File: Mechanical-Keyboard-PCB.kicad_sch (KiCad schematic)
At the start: 1 part, among them U1 ATmega32U4-A

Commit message: UCAP and HWB
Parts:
- added C2: C_Small, symbol Device:C_Small
- added R1: 10K, symbol Device:R_Small
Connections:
- net MOSI: now reaches U1.10 (PB2)
- net MISO: now reaches U1.11 (PB3)
- net RESET: now reaches U1.13 (~{RESET})
- net +5V: now reaches U1.14 (VCC), U1.34 (VCC)
- net +5V: now also U1.2 (UVCC), U1.24 (AVCC), U1.44 (AVCC)
- net GND: now reaches U1.15 (GND), U1.23 (GND), U1.35 (GND), U1.43 (GND)
- net GND: now also U1.5 (UGND), C2.2, R1.2
- net XTAL2: now reaches U1.16 (XTAL2)
- net XTAL1: now reaches U1.17 (XTAL1)
- net D-: now reaches U1.3 (D-)
- net at U1.33 (~{HWB}/PE2): now also R1.1
- net D+: now reaches U1.4 (D+)
- net at U1.6 (UCAP): now also C2.1
- net SCK: now reaches U1.9 (PB1)
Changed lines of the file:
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@@
 (kicad_sch (version 20230121) (generator eeschema)
   (paper "A4")
+  (junction (at 212.09 38.1) (diameter 0) (color 0 0 0 0)
+  )
+  (junction (at 209.55 129.54) (diameter 0) (color 0 0 0 0)
+  )
+  (junction (at 209.55 38.1) (diameter 0) (color 0 0 0 0)
+  )
+  (wire (pts (xy 212.09 38.1) (xy 214.63 38.1))
+    (stroke (width 0) (type default))
+  )
+  (wire (pts (xy 199.39 129.54) (xy 209.55 129.54))
+    (stroke (width 0) (type default))
+  )
+  (wire (pts (xy 248.92 99.06) (xy 261.62 99.06))
+    (stroke (width 0) (type default))
+  )
+  (wire (pts (xy 209.55 38.1) (xy 212.09 38.1))
+    (stroke (width 0) (type default))
+  )
+  (wire (pts (xy 199.39 134.62) (xy 199.39 129.54))
+    (stroke (width 0) (type default))
+  )
+  (wire (pts (xy 196.85 78.74) (xy 185.42 78.74))
+    (stroke (width 0) (type default))
+  )
+  (wire (pts (xy 209.55 33.02) (xy 209.55 38.1))
+    (stroke (width 0) (type default))
+  )
+  (wire (pts (xy 227.33 99.06) (xy 243.84 99.06))
+    (stroke (width 0) (type default))
+  )
+  (wire (pts (xy 261.62 99.06) (xy 261.62 101.6))
+    (stroke (width 0) (type default))
+  )
+  (wire (pts (xy 185.42 78.74) (xy 185.42 92.71))
+    (stroke (width 0) (type default))
+  )
+  (wire (pts (xy 209.55 129.54) (xy 212.09 129.54))
+    (stroke (width 0) (type default))
+  )
+  (hierarchical_label "MISO" (shape input) (at 227.33 53.34 0) (fields_autoplaced)
+    (effects (font (size 1.27 1.27)) (justify left))
+  )
+  (hierarchical_label "D+" (shape input) (at 196.85 71.12 180) (fields_autoplaced)
+    (effects (font (size 1.27 1.27)) (justify right))
+  )
+  (hierarchical_label "XTAL2" (shape input) (at 196.85 55.88 180) (fields_autoplaced)
+    (effects (font (size 1.27 1.27)) (justify right))
+  )
+  (hierarchical_label "D-" (shape input) (at 196.85 73.66 180) (fields_autoplaced)
+    (effects (font (size 1.27 1.27)) (justify right))
+  )
+  (hierarchical_label "XTAL1" (shape input) (at 196.85 50.8 180) (fields_autoplaced)
+    (effects (font (size 1.27 1.27)) (justify right))
+  )
+  (hierarchical_label "SCK" (shape input) (at 227.33 48.26 0) (fields_autoplaced)
+    (effects (font (size 1.27 1.27)) (justify left))
+  )
+  (hierarchical_label "RESET" (shape input) (at 196.85 45.72 180) (fields_autoplaced)
+    (effects (font (size 1.27 1.27)) (justify right))
+  )
+  (hierarchical_label "MOSI" (shape input) (at 227.33 50.8 0) (fields_autoplaced)
+    (effects (font (size 1.27 1.27)) (justify left))
+  )
+  (symbol (lib_id "Device:C_Small") (at 185.42 95.25 0) (unit 1)
+    (in_bom yes) (on_board yes) (dnp no) (fields_autoplaced)
+    (property "Reference" "C2" (at 187.96 94.6213 0)
+      (effects (font (size 1.27 1.27)) (justify left))
+    )
+    (property "Value" "C_Small" (at 187.96 97.1613 0)
+      (effects (font (size 1.27 1.27)) (justify left))
+    )
+    (property "Footprint" "" (at 185.42 95.25 0)
+      (effects (font (size 1.27 1.27)) hide)
+    )
+    (property "Datasheet" "~" (at 185.42 95.25 0)
+      (effects (font (size 1.27 1.27)) hide)
+    )
+    (pin "1")
+    (pin "2")
+    (instances
+      (project "Mechanical-Keyboard-PCB"
+        (path "/99e75afe-79a0-48d3-af4c-243d7dba3013"
+          (reference "C2") (unit 1)
+        )
+      )
+    )
+  )
+  (symbol (lib_id "power:GND") (at 261.62 101.6 0) (unit 1)
+    (in_bom yes) (on_board yes) (dnp no) (fields_autoplaced)
+    (property "Reference" "#PWR04" (at 261.62 107.95 0)
+      (effects (font (size 1.27 1.27)) hide)
+    )
+    (property "Value" "GND" (at 261.62 106.68 0)
+      (effects (font (size 1.27 1.27)))
+    )
+    (property "Footprint" "" (at 261.62 101.6 0)
+      (effects (font (size 1.27 1.27)) hide)
+    )
+    (property "Datasheet" "" (at 261.62 101.6 0)
+      (effects (font (size 1.27 1.27)) hide)
+    )
+    (pin "1")
+    (instances
+      (project "Mechanical-Keyboard-PCB"
+        (path "/99e75afe-79a0-48d3-af4c-243d7dba3013"
+          (reference "#PWR04") (unit 1)
+        )
+      )
+    )
+  )
+  (symbol (lib_id "power:+5V") (at 209.55 33.02 0) (unit 1)
+    (in_bom yes) (on_board yes) (dnp no) (fields_autoplaced)
+    (property "Reference" "#PWR01" (at 209.55 36.83 0)
+      (effects (font (size 1.27 1.27)) hide)
+    )
+    (property "Value" "+5V" (at 209.55 29.21 0)
+      (effects (font (size 1.27 1.27)))
+    )
+    (property "Footprint" "" (at 209.55 33.02 0)
+      (effects (font (size 1.27 1.27)) hide)
+    )
+    (property "Datasheet" "" (at 209.55 33.02 0)
+      (effects (font (size 1.27 1.27)) hide)
+    )
+    (pin "1")
+    (instances
+      (project "Mechanical-Keyboard-PCB"
+        (path "/99e75afe-79a0-48d3-af4c-243d7dba3013"
+          (reference "#PWR01") (unit 1)
+        )
+      )
+    )
+  )
+  (symbol (lib_id "Device:R_Small") (at 246.38 99.06 90) (unit 1)
+    (in_bom yes) (on_board yes) (dnp no) (fields_autoplaced)
+    (property "Reference" "R1" (at 246.38 93.98 90)
+      (effects (font (size 1.27 1.27)))
+    )
+    (property "Value" "10K" (at 246.38 96.52 90)
+      (effects (font (size 1.27 1.27)))
+    )
+    (property "Footprint" "" (at 246.38 99.06 0)
+      (effects (font (size 1.27 1.27)) hide)
+    )
+    (property "Datasheet" "~" (at 246.38 99.06 0)
+      (effects (font (size 1.27 1.27)) hide)
+    )
+    (pin "1")
+    (pin "2")
+    (instances
+      (project "Mechanical-Keyboard-PCB"
+        (path "/99e75afe-79a0-48d3-af4c-243d7dba3013"
+          (reference "R1") (unit 1)
+        )
+      )
+    )
+  )
   (symbol (lib_id "MCU_Microchip_ATmega:ATmega32U4-A") (at 212.09 83.82 0) (unit 1)
     (in_bom yes) (on_board yes) (dnp no) (fields_autoplaced)
@@
         )
       )
+    )
+  )
+  (symbol (lib_id "power:GND") (at 199.39 134.62 0) (unit 1)
+    (in_bom yes) (on_board yes) (dnp no) (fields_autoplaced)
+    (property "Reference" "#PWR02" (at 199.39 140.97 0)
+      (effects (font (size 1.27 1.27)) hide)
+    )
+    (property "Value" "GND" (at 199.39 139.7 0)
+      (effects (font (size 1.27 1.27)))
+    )
+    (property "Footprint" "" (at 199.39 134.62 0)
+      (effects (font (size 1.27 1.27)) hide)
+    )
+    (property "Datasheet" "" (at 199.39 134.62 0)
+      (effects (font (size 1.27 1.27)) hide)
+    )
+    (pin "1")
+    (instances
+      (project "Mechanical-Keyboard-PCB"
+        (path "/99e75afe-79a0-48d3-af4c-243d7dba3013"
+          (reference "#PWR02") (unit 1)
+        )
+      )
+    )
+  )
+  (symbol (lib_id "power:GND") (at 185.42 97.79 0) (unit 1)
+    (in_bom yes) (on_board yes) (dnp no) (fields_autoplaced)
+    (property "Reference" "#PWR03" (at 185.42 104.14 0)
+      (effects (font (size 1.27 1.27)) hide)
+    )
+    (property "Value" "GND" (at 185.42 102.87 0)
+      (effects (font (size 1.27 1.27)))
+    )
+    (property "Footprint" "" (at 185.42 97.79 0)
+      (effects (font (size 1.27 1.27)) hide)
+    )
+    (property "Datasheet" "" (at 185.42 97.79 0)
+      (effects (font (size 1.27 1.27)) hide)
+    )
+    (pin "1")
+    (instances
+      (project "Mechanical-Keyboard-PCB"
+        (path "/99e75afe-79a0-48d3-af4c-243d7dba3013"
+          (reference "#PWR03") (unit 1)
+        )
+      )

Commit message: Crystal, decoupling capacitors + ISP
Crystal, decoupling capacitors + ISP
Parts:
- added C1, C3: 22p, symbol Device:C_Small
- added C1, C2, C3, C4: 0.1u, symbol Device:C_Small
- added C5: 10u, symbol Device:C_Small
- added J1: AVR-ISP-6, symbol Connector:AVR-ISP-6
- added XTAL: X?, symbol Device:Crystal_GND24_Small
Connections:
- net +5V: now also C1.1, C1.2, C1.2, C2.1, C2.2, C3.1, C3.2, C3.2, C4.1, C4.2, C5.1, C5.2, J1.2 (VCC), J1.6 (GND), XTAL.2, XTAL.4
- net MISO: now also J1.1 (MISO)
- net MOSI: now also J1.4 (MOSI)
- net RESET: now also J1.5 (~{RST})
- net SCK: now also J1.3 (SCK)
- net XTAL1: now also C1.1, XTAL.1
- net XTAL2: now also C3.1, XTAL.3
- no-connect marks 0 -> 1

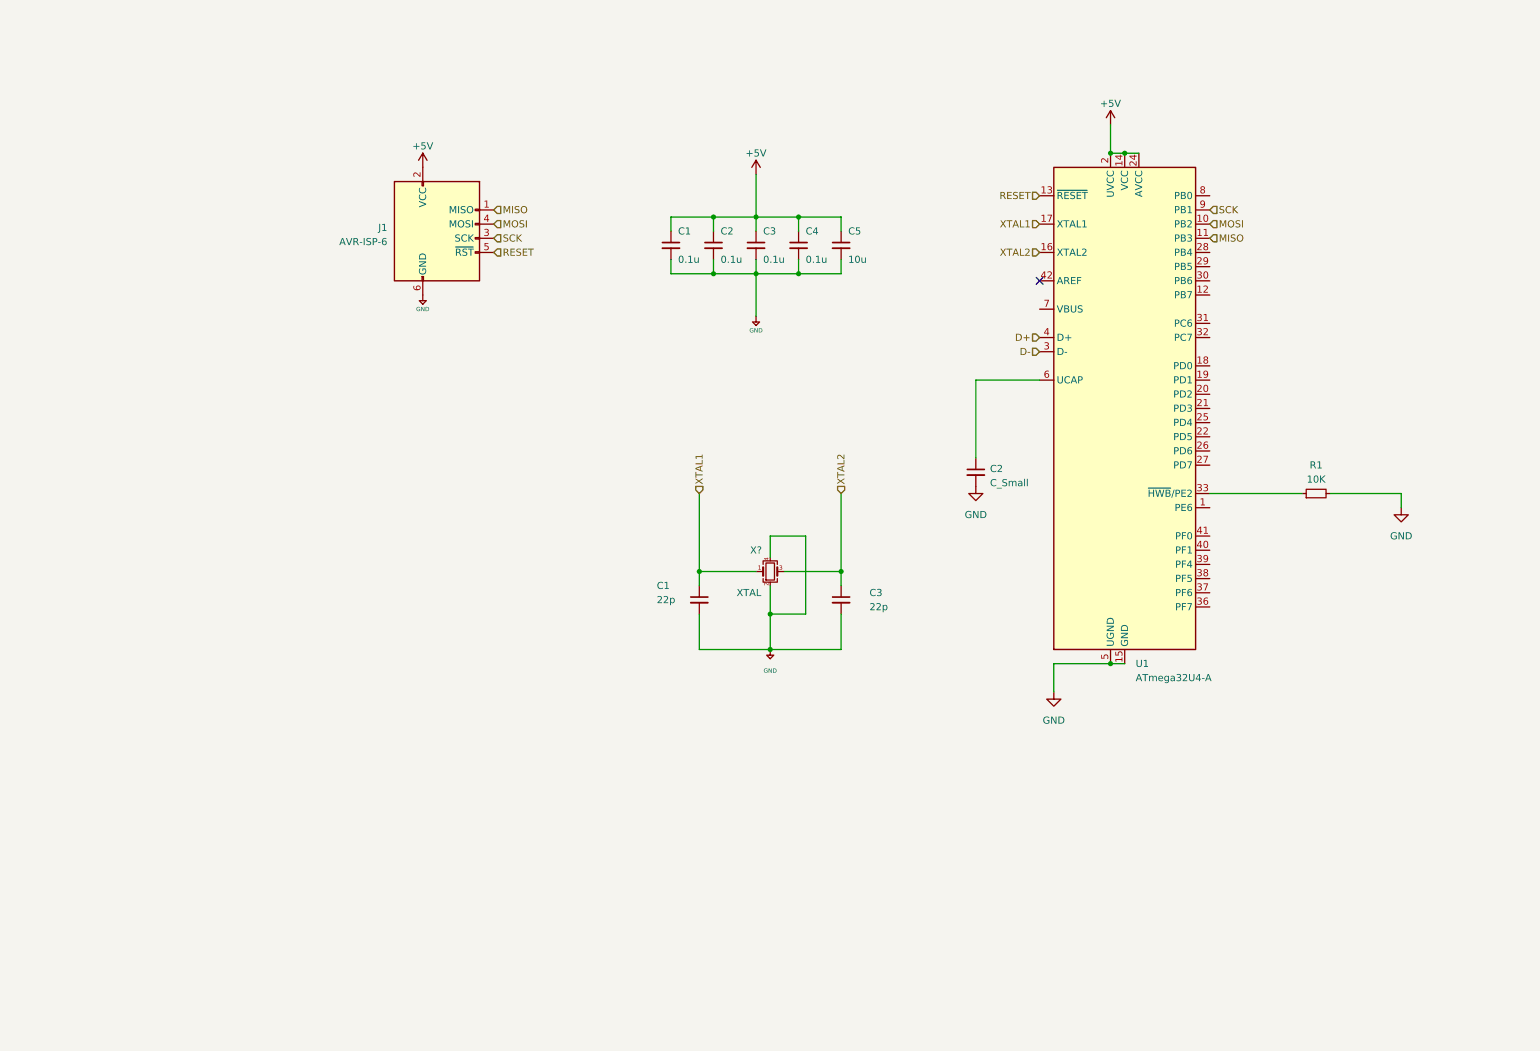
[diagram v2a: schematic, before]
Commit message: Schematic - USB, EMI + RESET
Added USB, EMI + RESET to the schematic
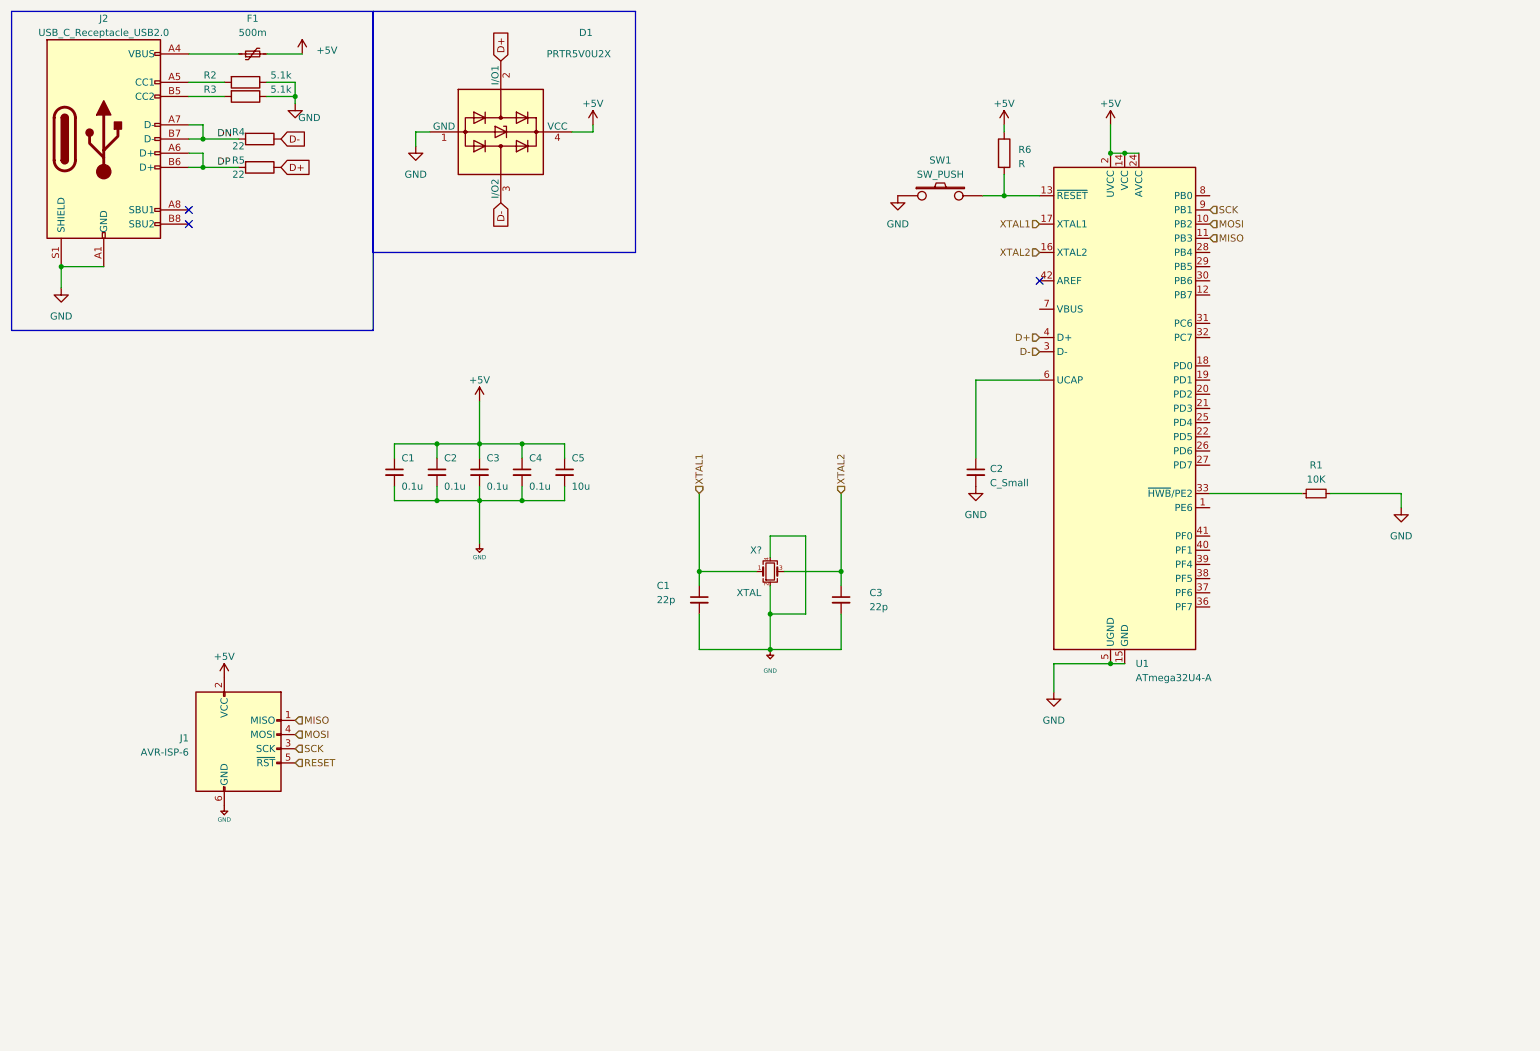
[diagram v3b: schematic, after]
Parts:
- added D1: PRTR5V0U2X, Package_TO_SOT_SMD:SOT-143, symbol Power_Protection:PRTR5V0U2X
- added F1: 500m, symbol Device:Polyfuse_Small
- added J2: USB_C_Receptacle_USB2.0, symbol Connector:USB_C_Receptacle_USB2.0
- added R2, R3: 5.1k, Resistor_SMD:R_0805_2012Metric_Pad1.20x1.40mm_HandSolder, symbol Device:R
- added R4, R5: 22, Resistor_SMD:R_0805_2012Metric_Pad1.20x1.40mm_HandSolder, symbol Device:R
- added R6: R, symbol Device:R
- added SW1: SW_PUSH, symbol keyboard_parts:SW_PUSH
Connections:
- net +5V: now also D1.4 (VCC), F1.2, R6.1
- net D+: now also D1.2 (I/O1), R5.1
- net D-: now also D1.3 (I/O2), R4.1
- net GND: now also D1.1 (GND), J2.A1 (GND), J2.A12 (GND), J2.B1 (GND), J2.B12 (GND), J2.S1 (SHIELD), R2.1, R3.1, SW1.1
- net RESET: no longer U1.13 (~{RESET})
- new net: F1.1, J2.A4 (VBUS), J2.A9 (VBUS), J2.B4 (VBUS), J2.B9 (VBUS)
- new net: J2.A5 (CC1), R2.2
- new net: J2.B5 (CC2), R3.2
- new net: R6.2, SW1.2, U1.13 (~{RESET})
- new net DN: J2.A7 (D-), J2.B7 (D-), R4.2
- new net DP: J2.A6 (D+), J2.B6 (D+), R5.2
- no-connect marks 1 -> 3
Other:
- moved on the sheet: C1, C2, C3, C4, C5, J1

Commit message: Crystal update and start matrix
Separate ground on crystal shunt capacitors and begin matrix
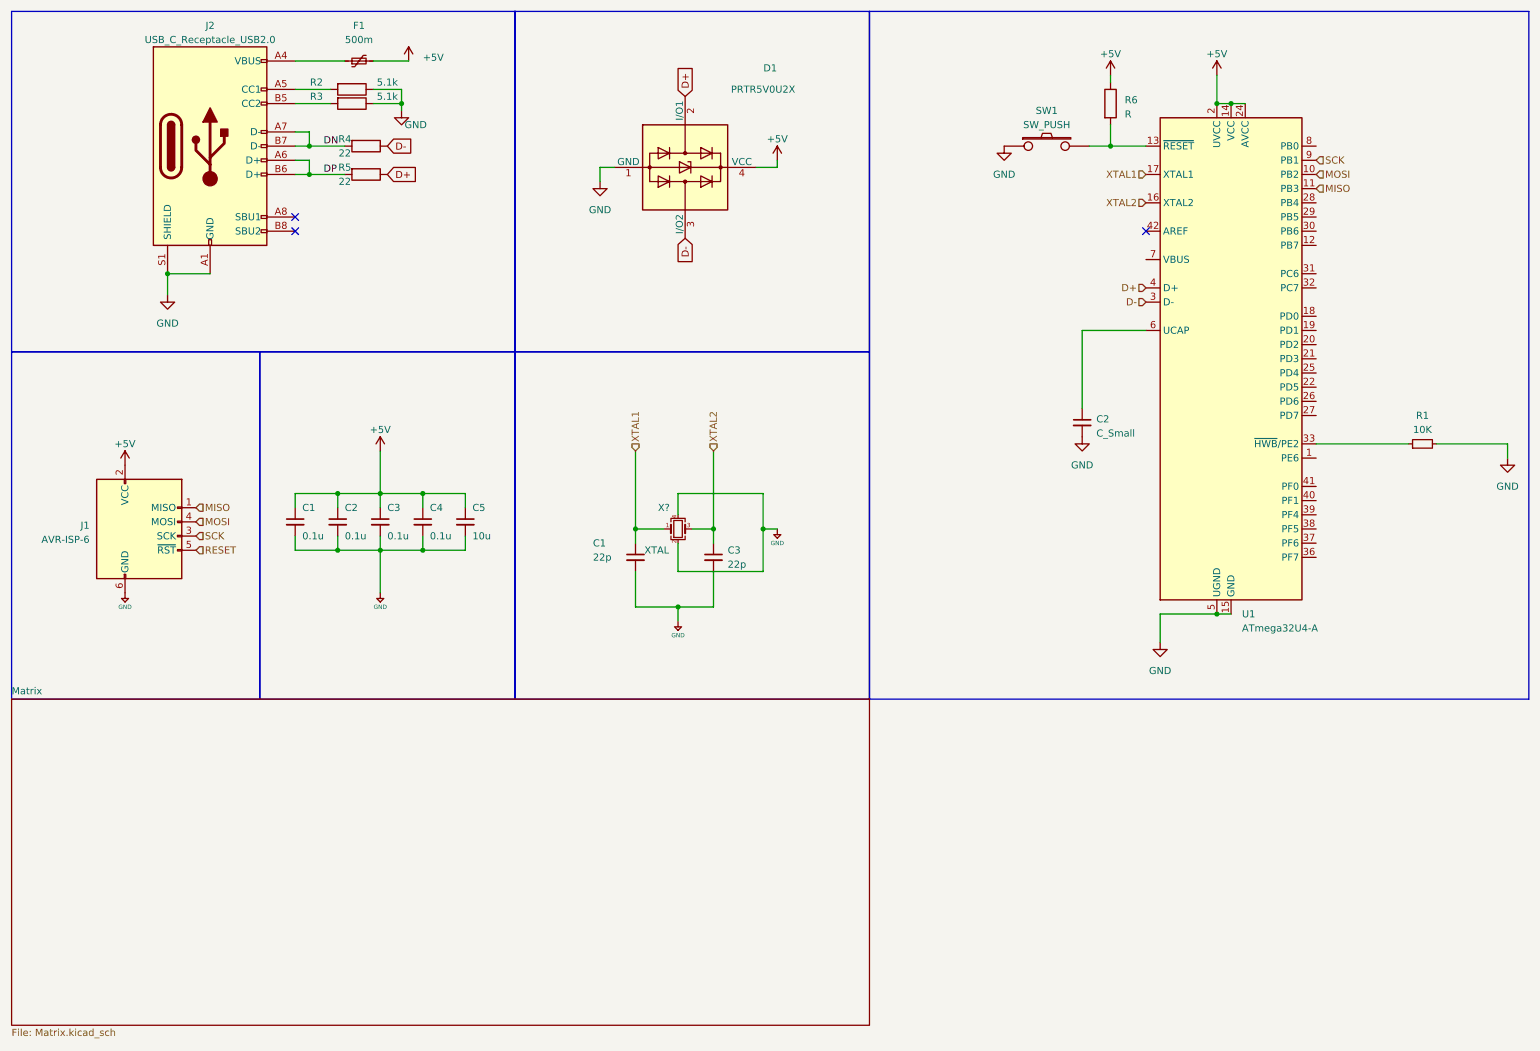
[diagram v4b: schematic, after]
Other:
- added sheet Matrix (Matrix.kicad_sch)
- moved on the sheet: C1, C2, C3, C4, C5, D1, F1, J1, J2, R1, R2, R3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
